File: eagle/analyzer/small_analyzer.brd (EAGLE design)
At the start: 82.5 x 34.3 mm, 37 parts, among them IC1 MCP604ST, IC2 TPS77301, IC3 TPS77350, U1 AD5933, U2 ATMEGA328P

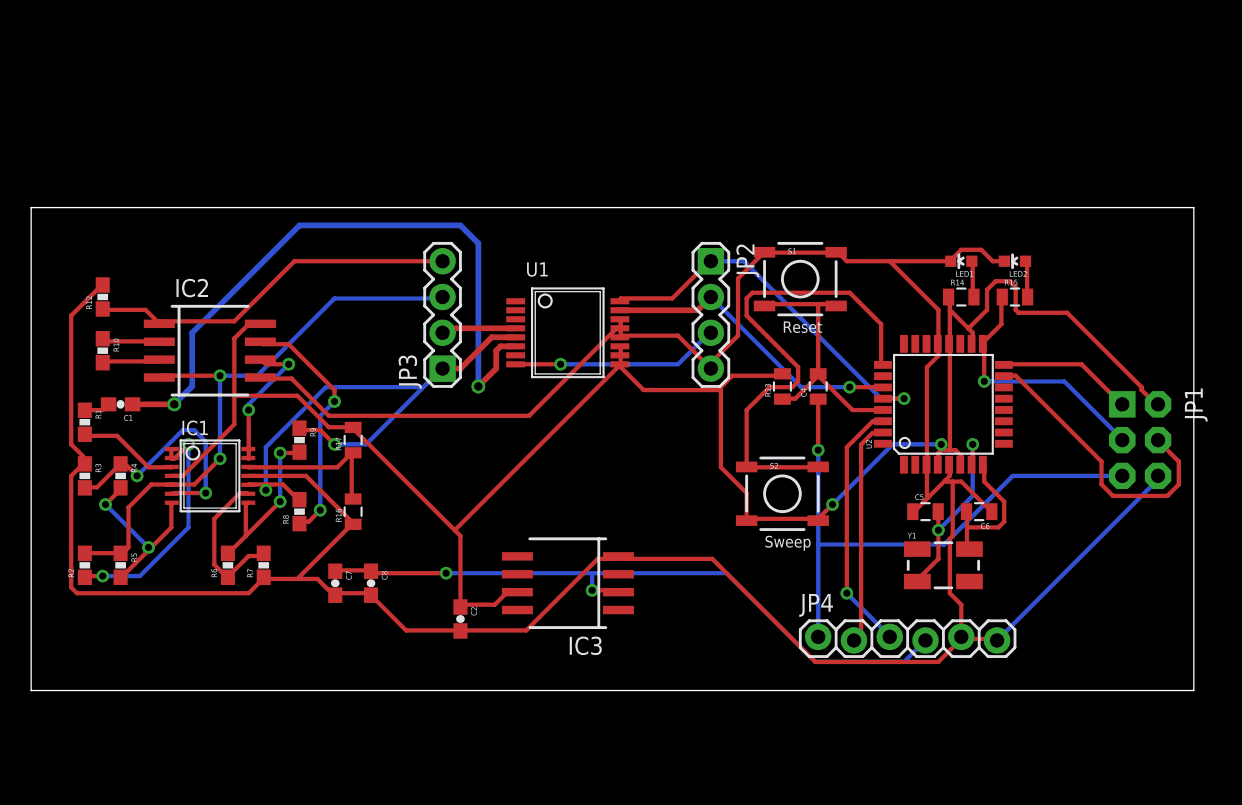
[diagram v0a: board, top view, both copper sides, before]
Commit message: added sweep push button and decoupling caps
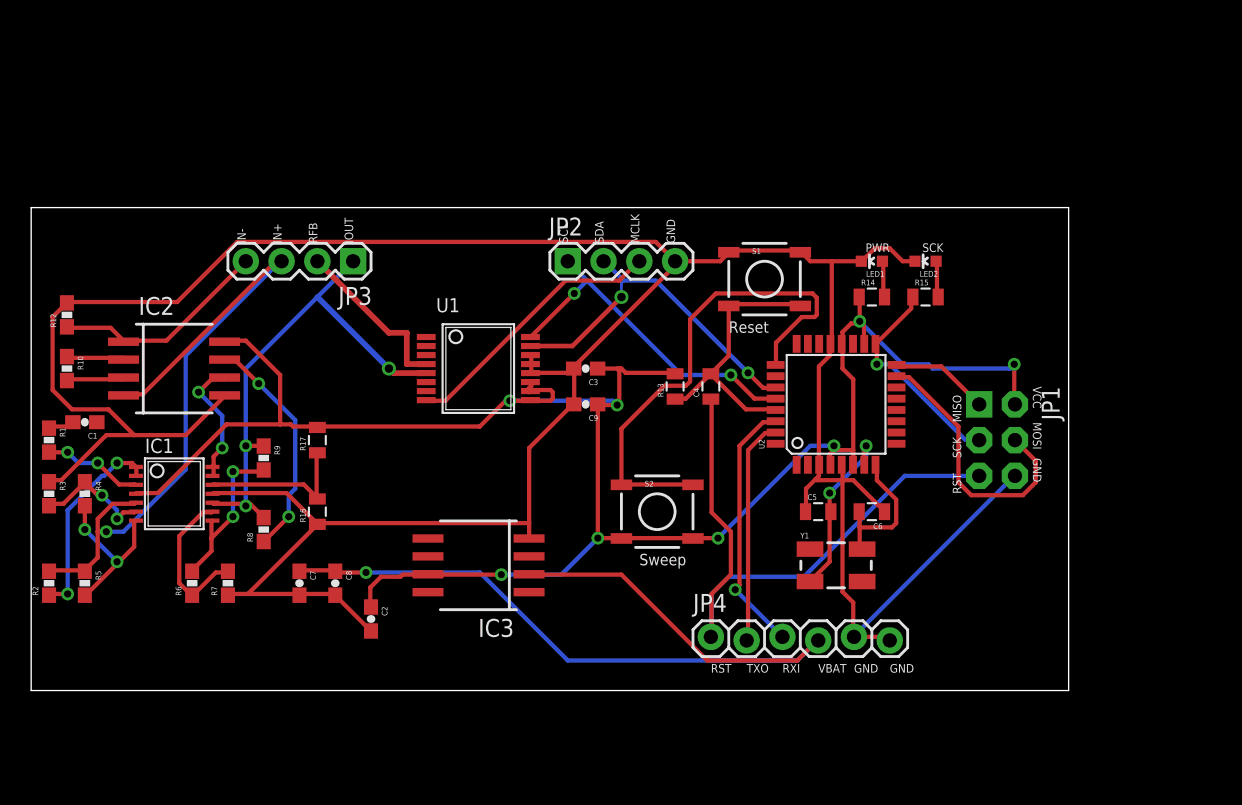
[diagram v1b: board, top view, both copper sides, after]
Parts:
- added C3: 10uF, SparkFun-Passives:0603-CAP
- added C9: 0.1uF, SparkFun-Passives:0603-CAP
- R4: value 150k -> 100k
- R5: value 66.5k -> 100k
- moved JP1 10.2 mm to (68.6, 17.8)
- moved JP2 10.2 mm to (38.1, 30.5), turned to 0 degrees
- moved JP3 9.92 mm to (22.9, 30.5), turned to 180 degrees
- moved S2 8.98 mm to (44.5, 12.7)
- moved C4 7.62 mm to (48.3, 21.6)
- moved C6 7.62 mm to (59.7, 12.7)
- moved JP4 7.62 mm to (48.3, 3.81)
- moved R13 7.62 mm to (45.7, 21.6)
- moved C5 7.62 mm to (55.9, 12.7)
- moved U2 7.62 mm to (57.1, 20.3)
- moved Y1 7.62 mm to (57.1, 8.89)
- moved U1 6.84 mm to (31.8, 22.9)
- moved IC3 6.48 mm to (31.8, 8.89)
- moved LED1 6.35 mm to (59.7, 30.5)
- moved R14 6.35 mm to (59.7, 27.9)
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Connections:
- net GND: now also C3.2, C9.2
- net VCC: now also C3.1, C9.1
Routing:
- net VIN: track 47.3 -> 0.00 mm, vias 2 -> 0
- net VBAT: track 48.5 -> 63.8 mm, vias 2 -> 1
- net GND: track 233.4 -> 219.7 mm
- net -IN: track 26.5 -> 15.5 mm
- net N$5: track 17.5 -> 8.54 mm
- net +IN: track 42.5 -> 50.7 mm, vias 2 -> 1
- net RFB: track 5.32 -> 12.1 mm
- net MCLK: track 14.8 -> 19.2 mm, vias 1 -> 0
- net VCC: track 139.4 -> 142.9 mm, vias 2 -> 8
- net IOUT2: track 39.4 -> 36.0 mm, vias 2 -> 3
- net SDA: track 21.7 -> 25.1 mm, vias 1 -> 2
- net RST: track 40.5 -> 43.6 mm, vias 1 -> 0
- net N$3: track 17.1 -> 14.3 mm
- net SCK: track 18.2 -> 15.4 mm
- net MISO: track 9.61 -> 7.02 mm
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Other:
- board size 82.5 x 34.3 mm -> 73.7 x 34.3 mm
- board text added: "GND"
- board text added: "IN+"
- board text added: "IN-"
- board text added: "IOUT"
- board text added: "MCLK"
- board text added: "MISO"
- board text added: "MOSI"
- board text added: "PWR"
- board text added: "RFB"
- board text added: "RST"
- board text added: "RXI"
- board text added: "SCK"
- board text added: "SCL"
- board text added: "SDA"
- board text added: "TXO"
- board text added: "VBAT"
- board text added: "VCC"

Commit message: added dual voltage regulator to board
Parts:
- added IC4: (no value), AWJLEagleLib:DFN14-4X3DE
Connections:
- new net IN: IC4.6, IC4.9
- new net IP: IC4.14
- new net ON: IC4.7
- new net OP: IC4.1
- net GND: now also IC4.4, IC4.5
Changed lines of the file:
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@@
 <?xml version="1.0" encoding="utf-8"?>
 <!DOCTYPE eagle SYSTEM "eagle.dtd">
-<eagle version="6.5.0">
+<eagle version="6.4">
 <drawing>
 <settings>
@@
 <element name="C3" library="SparkFun-Passives" package="0603-CAP" value="10uF" x="39.37" y="22.86" rot="R180"/>
 <element name="C9" library="SparkFun-Passives" package="0603-CAP" value="0.1uF" x="39.37" y="20.32" rot="R180"/>
+<element name="IC4" library="AWJLEagleLib" package="DFN14-4X3DE" value="" x="3.81" y="-3.81"/>
 </elements>
 <signals>
@@
 <wire x1="57.6072" y1="14.9352" x2="57.6072" y2="7.0104" width="0.3048" layer="1"/>
 <wire x1="58.3692" y1="3.81" x2="58.42" y2="3.81" width="0.3048" layer="1"/>
+<contactref element="IC4" pad="4"/>
+<contactref element="IC4" pad="5"/>
+<wire x1="3.81" y1="-4.56" x2="13.97" y2="6.77" width="0" layer="19" extent="1-1"/>
+<wire x1="4.31" y1="-5.21" x2="3.81" y2="-4.56" width="0" layer="19" extent="1-1"/>
 </signal>
 <signal name="VIN">
@@
 <wire x1="41.91" y1="14.6304" x2="41.91" y2="14.605" width="0.3048" layer="1"/>
 </signal>
+<signal name="OP">
+<contactref element="IC4" pad="1"/>
+</signal>
+<signal name="IN">
+<contactref element="IC4" pad="6"/>
+<contactref element="IC4" pad="9"/>
+<wire x1="4.81" y1="-3.06" x2="4.81" y2="-5.21" width="0" layer="19" extent="1-1"/>
+</signal>
+<signal name="ON">
+<contactref element="IC4" pad="7"/>
+</signal>
+<signal name="IP">
+<contactref element="IC4" pad="14"/>
+</signal>
 </signals>
-<errors>
-</errors>
 </board>
 </drawing>

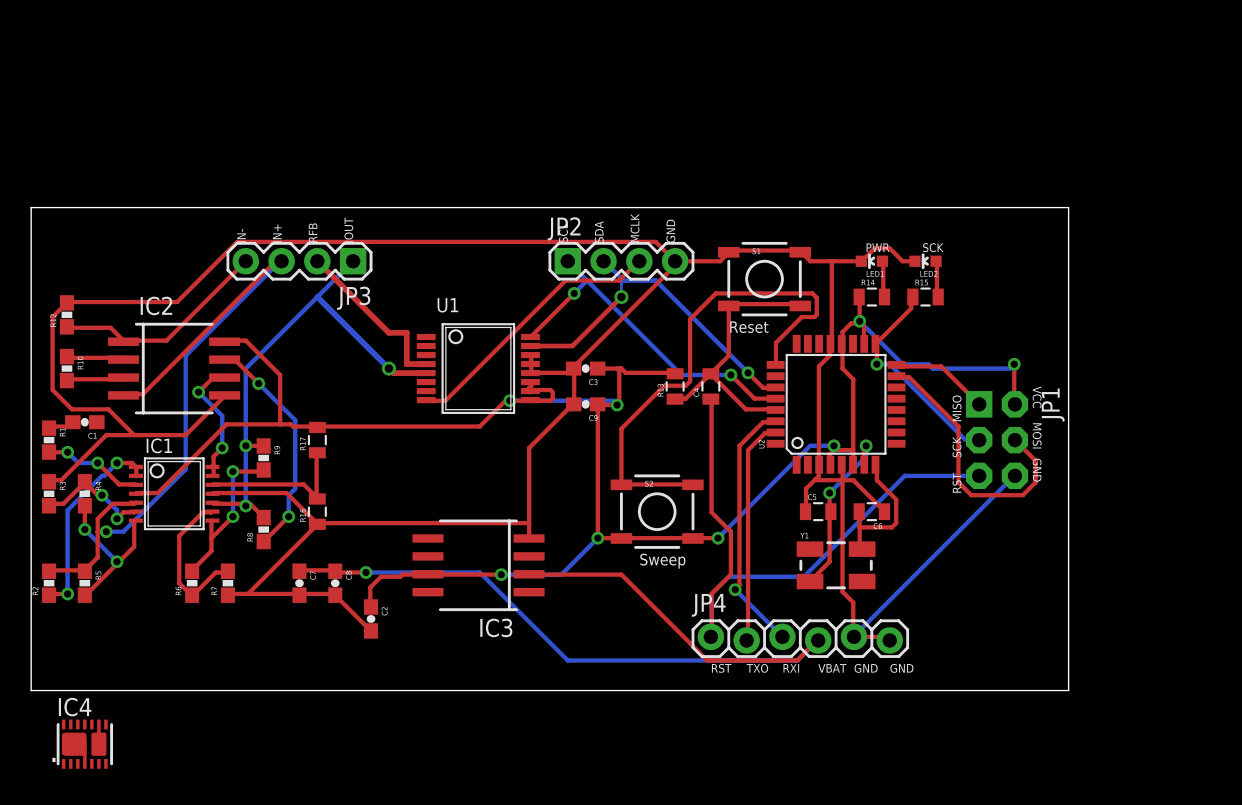
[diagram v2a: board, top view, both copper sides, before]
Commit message: updated schematic to dual voltage regulator, errors in board
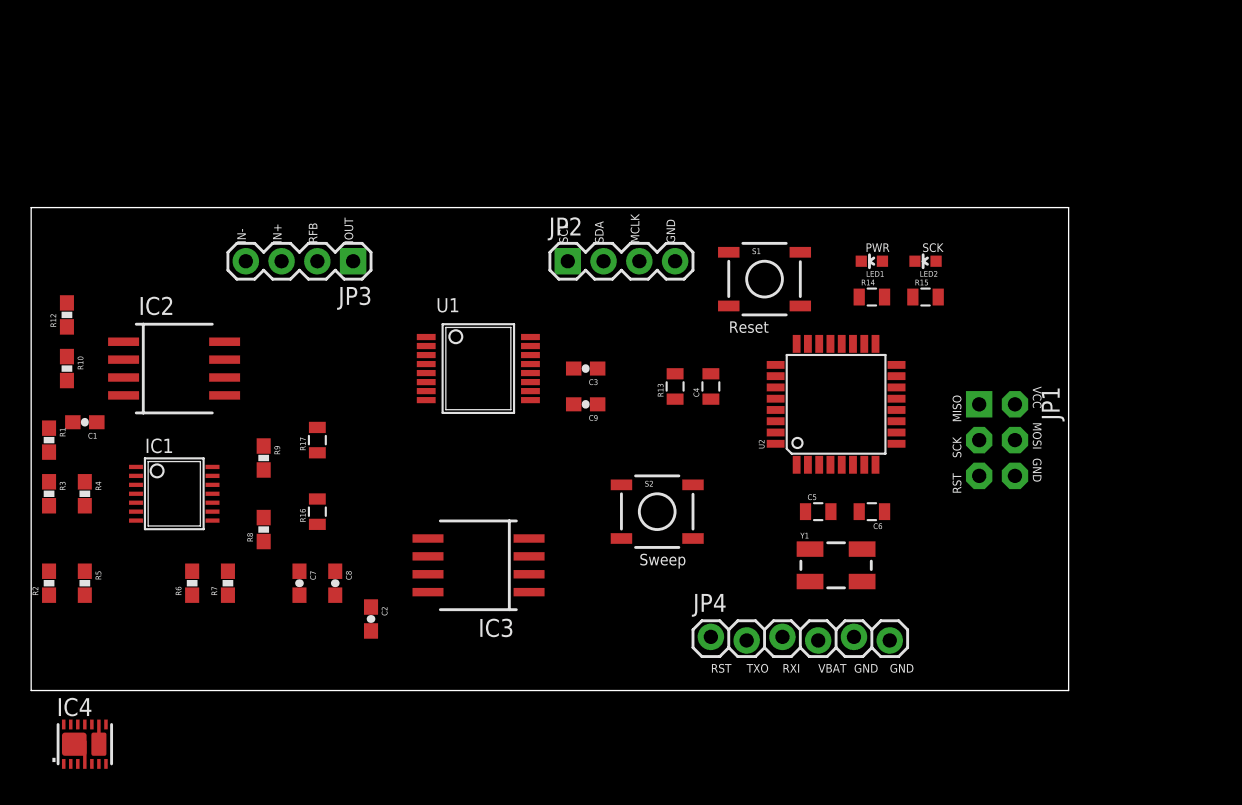
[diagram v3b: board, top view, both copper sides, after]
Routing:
- net GND: track 219.7 -> 0.00 mm
- net VCC: track 142.9 -> 0.00 mm, vias 8 -> 0
- net VBAT: track 63.8 -> 0.00 mm, vias 1 -> 0
- net +IN: track 50.7 -> 0.00 mm, vias 1 -> 0
- net RST: track 43.6 -> 0.00 mm
- net N$16: track 36.1 -> 0.00 mm
- net IOUT2: track 36.0 -> 0.00 mm, vias 3 -> 0
- net SDA: track 25.1 -> 0.00 mm, vias 2 -> 0
- net SCL: track 24.5 -> 0.00 mm, vias 2 -> 0
- net MOSI: track 19.7 -> 0.00 mm
- net N$11: track 19.6 -> 0.00 mm
- net MCLK: track 19.2 -> 0.00 mm
- net RXI: track 18.4 -> 0.00 mm, vias 1 -> 0
- net VAMP: track 16.3 -> 0.00 mm, vias 2 -> 0
- net TXO: track 16.0 -> 0.00 mm
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
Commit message: analyzer version 1 as submitted for pcb fab
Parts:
- removed C8: 0.1uF, SparkFun-Passives:0603-CAP
- removed IC3: TPS77350, texas:SOP-08
- added BAT1: +3V, SparkFun-Electromechanical:BATTCON_12MM
- added BAT2: -3V, SparkFun-Electromechanical:BATTCON_12MM
- added C10, C11, C12, C13: 10uF, SparkFun-Passives:0603-CAP
- added C14, C15: 0.01uF, SparkFun-Passives:0603-CAP
- added JP6: M02PTH, SparkFun-Connectors:1X02
- added R1N, R1P, R2N, R2P: 100k, SparkFun-Passives:0805
- added U$1, U$2, U$3, U$4: (no value), SparkFun-Electromechanical:STAND-OFF
- C2: value 0.1uF -> 1u
- C7: value 10uF -> 1u
- moved IC4 35.4 mm to (36.8, 8.89)
- moved C7 28.1 mm to (10.2, 34.3), turned to 90 degrees
- moved C2 24.7 mm to (10.2, 25.4), turned to 180 degrees
- moved R12 13.7 mm to (10.2, 38.1)
- moved S1 12.0 mm to (55.9, 40.6)
- moved JP3 12.0 mm to (26.7, 41.9)
- moved LED1 12.0 mm to (63.5, 41.9)
- moved LED2 12.0 mm to (67.3, 41.9)
- moved R14 12.0 mm to (63.5, 39.4)
- moved R15 12.0 mm to (67.3, 39.4)
- moved JP2 12.0 mm to (41.9, 41.9)
- moved IC2 8.98 mm to (16.5, 29.2)
- moved R10 8.98 mm to (8.89, 29.2)
- moved S2 6.84 mm to (47.0, 19.1)
- moved C3 6.48 mm to (40.6, 29.2)
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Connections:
- net IOUT2 renamed IIN
- net VREF renamed VDC
- removed net +IN: IC1.5, IC2.4, JP3.3, R2.2, R5.1
- removed net -IN: IC2.1, JP3.4, R12.1
- removed net CS: U2.14
- removed net IN: IC4.6, IC4.9
- removed net IP: IC4.14
- removed net N$17: U2.23
- removed net ON: IC4.7
- removed net OP: IC4.1
- new net +IOUT: C2.1, IC1.5, JP3.3, R2.2, R5.1
- new net -IOUT: C7.2, JP3.4, R12.1
- new net -VCC: C13.1, C15.1, IC4.7, R2N.2
- new net A1: JP6.2, U2.24
- new net D6: JP6.1, U2.10
- new net N$14: BAT1.GND, BAT2.PWR@1, C10.1, C11.2, IC4.4
- new net N$19: BAT2.GND, C10.2, IC4.10, IC4.6, IC4.9
- new net N$20: C14.2, IC4.3
- new net N$21: C15.2, IC4.11
- new net N$22: IC4.8, R1N.2, R2N.1
- new net N$23: IC4.2, R1P.1, R2P.2
- new net N$24: C7.1, IC2.1
- new net N$25: C2.2, IC2.4
- net GND: now also C12.2, C13.2, R1N.1, R1P.2; no longer C2.2, C7.2, C8.2, IC3.4, IC4.4
- net VBAT: now also BAT1.PWR@1, C11.1, IC4.12, IC4.14; no longer C7.1, C8.1, IC3.2
- net VCC: now also C12.1, C14.1, IC4.1, R2P.1; no longer C2.1, IC3.7
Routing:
- net GND: track 0.00 -> 234.9 mm, vias 0 -> 2
- net VCC: track 0.00 -> 152.4 mm, vias 0 -> 4
- net VBAT: track 0.00 -> 86.3 mm, vias 0 -> 1
- net N$14: track 0.00 -> 72.2 mm, vias 0 -> 3
- net +IOUT: track 0.00 -> 68.5 mm
- net IIN: track 0.00 -> 65.3 mm, vias 0 -> 6
- net N$19: track 0.00 -> 51.4 mm, vias 0 -> 1
- net RST: track 0.00 -> 43.1 mm, vias 0 -> 1
- net SCK: track 0.00 -> 35.2 mm, vias 0 -> 1
- net SDA: track 0.00 -> 34.6 mm, vias 0 -> 1
- net SCL: track 0.00 -> 32.9 mm, vias 0 -> 1
- net RXI: track 0.00 -> 32.7 mm, vias 0 -> 1
- net VIN: track 0.00 -> 29.2 mm, vias 0 -> 2
- net TXO: track 0.00 -> 28.6 mm, vias 0 -> 1
- net MCLK: track 0.00 -> 28.4 mm
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- added copper zone on layer 1, net GND
- added copper zone on layer 16, net GND
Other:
- board size 73.7 x 34.3 mm -> 73.7 x 47 mm
- board text added: "A1"
- board text added: "D6"
- board text added: "ImpedanceAnalyzer_v1.0"
- board text added: "THAYER SCHOOL OF ENGINEERING"
